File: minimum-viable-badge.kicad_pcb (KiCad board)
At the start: 2 copper layers, 120 x 64 mm, 67 parts, among them J101 EDGE_CONNECTOR, P101 USB, P102 BATTERY, P103 POT_LONG, P104 BUTTON_A, P105 BUTTON_B, P106 POT_SHORT, P107 MECH, P108 MECH, P109 MECH, P301 eInk, Q101 S8050, Q102 S8050, Q201 FDN340P, Q301 IRLML0030TRPBF, SW101 PRGM, SW102 RESET, SW201 ON|OFF, U101 ESP32-WROOM, U102 CP2102, U201 MCP73831, U202 NCP5501

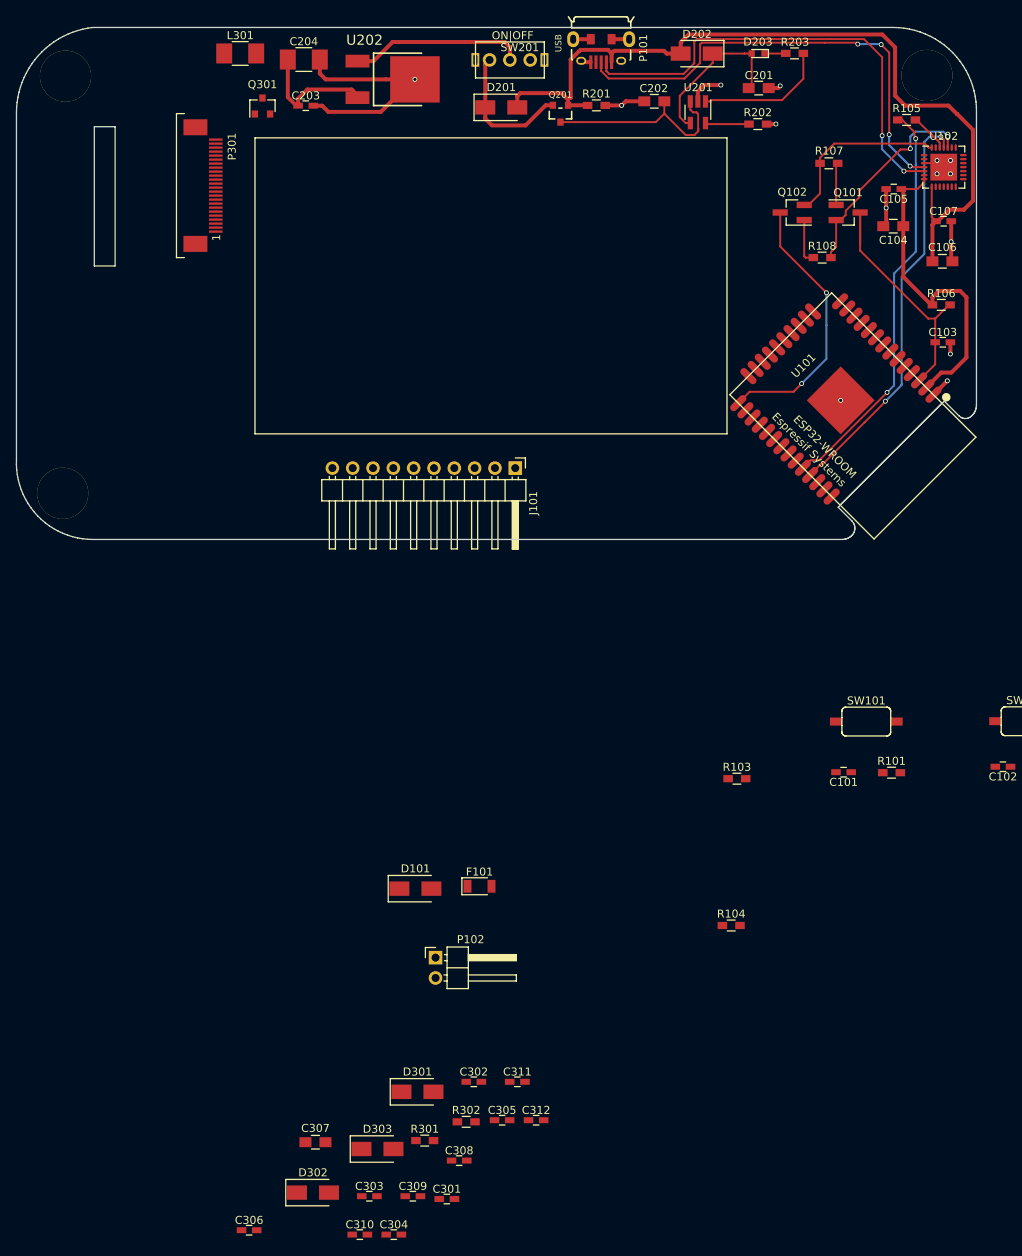
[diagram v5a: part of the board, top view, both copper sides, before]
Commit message: many more components added to the pcb
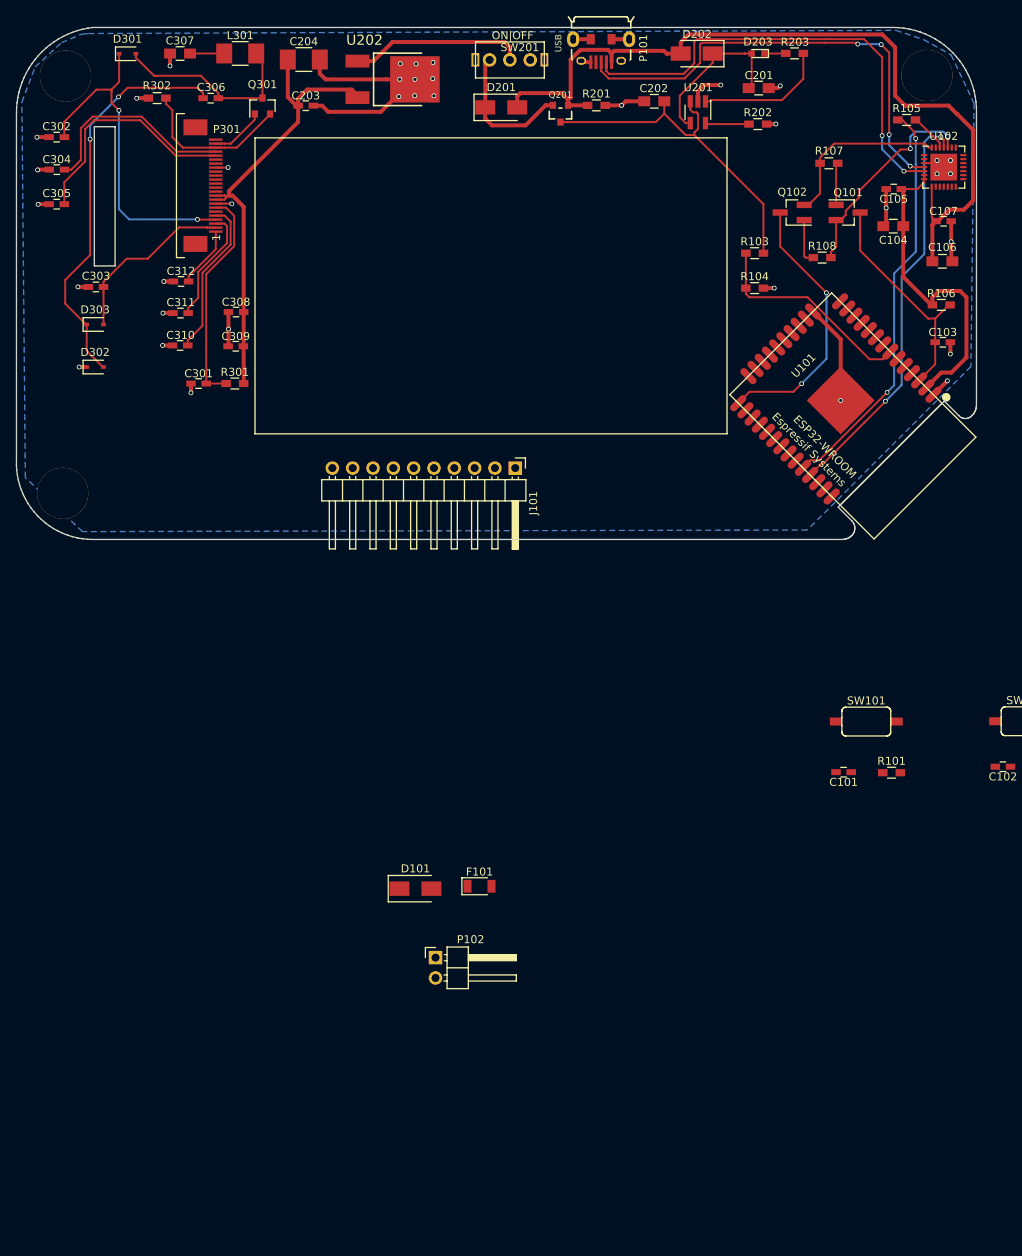
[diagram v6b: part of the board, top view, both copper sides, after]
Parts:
- D301, D302, D303: value SS14 -> SD103AWS; footprint Diodes_SMD:D_SMA -> Diodes_SMD:D_SOD-323
- moved C306 141.6 mm to (44.3, 44.8), turned to 180 degrees
- moved C304 139.6 mm to (25.1, 53.8), turned to 180 degrees
- moved C307 137.1 mm to (40.5, 39.3), turned to 180 degrees
- moved D301 134.7 mm to (33.9, 39.3)
- moved R302 133.7 mm to (37.6, 44.8), turned to 180 degrees
- moved C302 129.1 mm to (25.0, 49.7), turned to 180 degrees
- moved C305 127.3 mm to (25.0, 58.1), turned to 180 degrees
- moved C303 118.7 mm to (29.9, 68.4), turned to 180 degrees
- moved C312 113.9 mm to (40.6, 67.8), turned to 180 degrees
- moved C310 113.4 mm to (40.5, 75.8), turned to 180 degrees
- moved C308 109.7 mm to (47.5, 71.6)
- moved D303 108.9 mm to (29.8, 73.1)
- moved C309 108.5 mm to (47.4, 75.8)
- moved D302 106.7 mm to (29.8, 78.5)
- moved C301 106.6 mm to (42.8, 80.5)
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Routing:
- net Net-(C306-Pad2): track 0.00 -> 50.6 mm, vias 0 -> 2
- net +3V3: track 56.0 -> 98.8 mm
- net /E-Ink Display/PREVGH: track 0.00 -> 42.3 mm, vias 0 -> 2
- net GND: track 62.1 -> 98.4 mm, vias 14 -> 37
- net /E-Ink Display/VGH: track 0.00 -> 29.1 mm
- net /E-Ink Display/LCD_VDD: track 0.00 -> 27.6 mm
- net /BAT_MON: track 0.00 -> 26.9 mm
- net /E-Ink Display/VGL: track 0.00 -> 25.8 mm
- net Net-(C306-Pad1): track 0.00 -> 24.7 mm
- net /E-Ink Display/PREVGL: track 0.00 -> 22.2 mm
- net /E-Ink Display/VSH: track 0.00 -> 19.9 mm
- net /E-Ink Display/RESE: track 0.00 -> 19.7 mm
- net /BAT+: track 24.9 -> 43.2 mm
- net /E-Ink Display/VSL: track 0.00 -> 14.4 mm
- net /E-Ink Display/VCOM: track 0.00 -> 7.64 mm
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- added copper zone on B.Cu, net GND

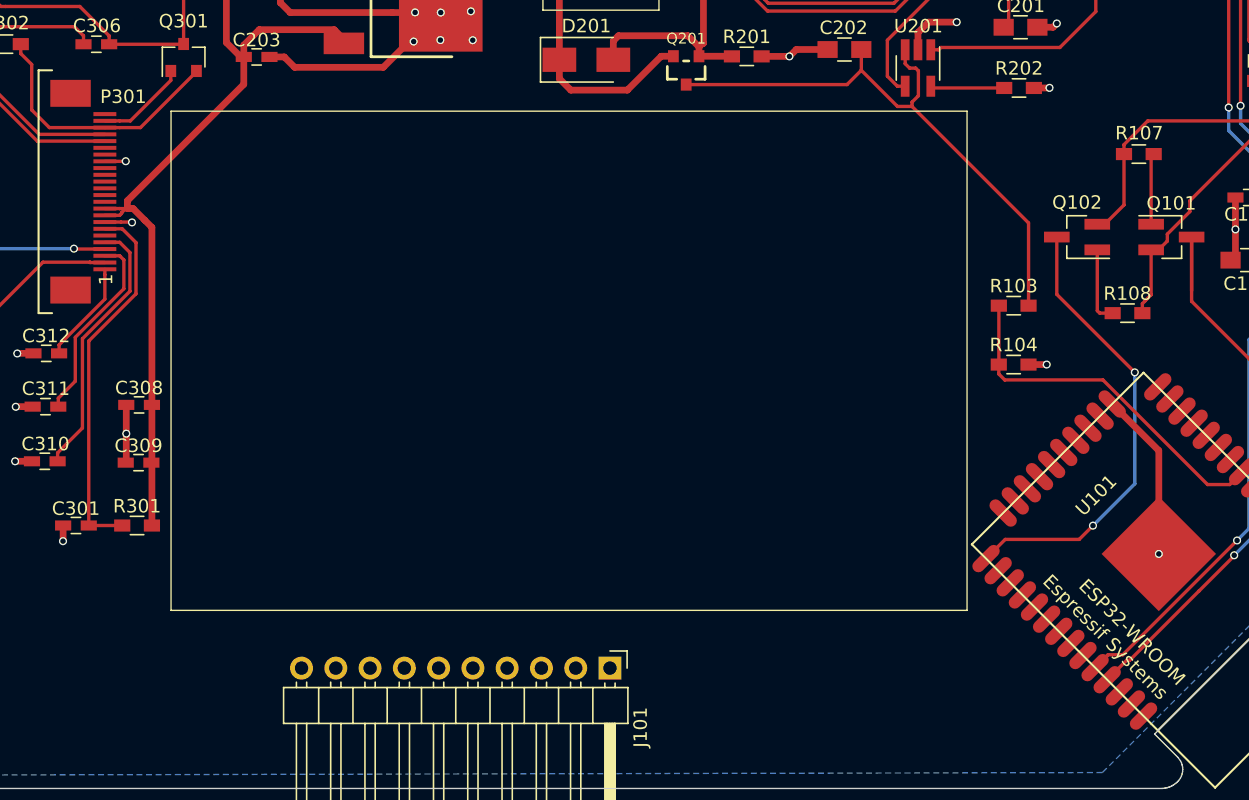
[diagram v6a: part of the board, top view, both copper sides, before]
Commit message: LCD pins routed to ESP32
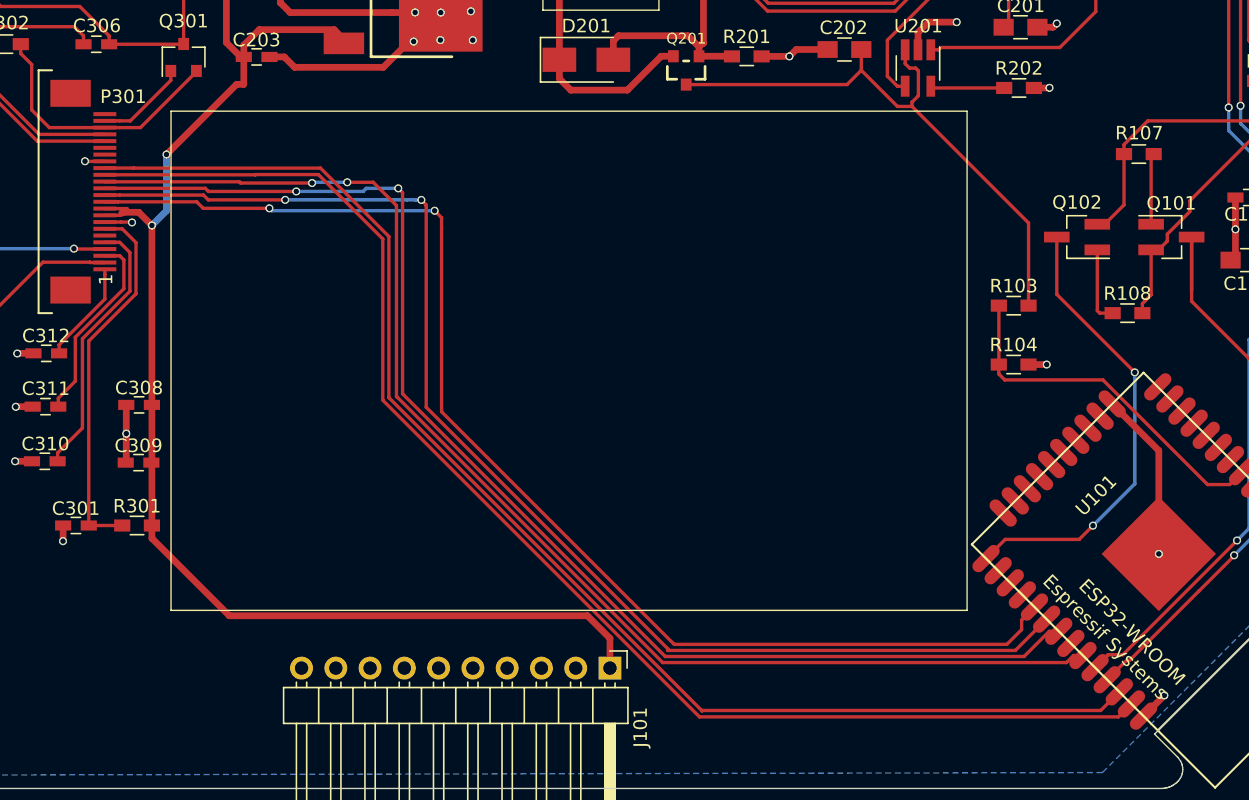
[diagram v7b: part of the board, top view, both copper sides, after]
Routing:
- net /EINK_RST: track 0.00 -> 100.1 mm
- net /EINK_BUSY: track 0.00 -> 99.4 mm
- net /EINK_D/C: track 0.00 -> 95.8 mm, vias 0 -> 2
- net /EINK_CS: track 0.00 -> 94.8 mm, vias 0 -> 2
- net /EINK_SCLK: track 0.00 -> 93.6 mm, vias 0 -> 2
- net /EINK_MOSI: track 0.00 -> 92.5 mm, vias 0 -> 2
- net +3V3: track 98.8 -> 140.2 mm, vias 0 -> 2
- net GND: track 98.4 -> 100.5 mm, vias 37 -> 38

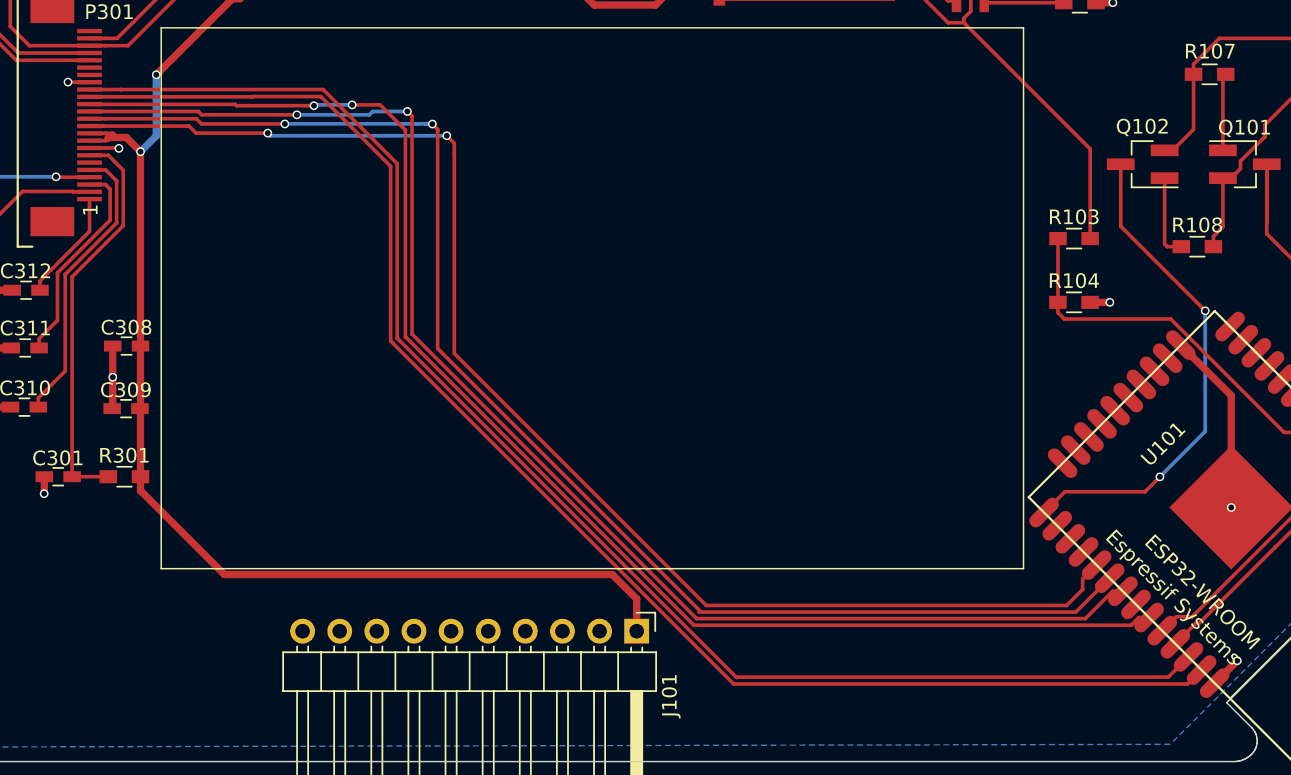
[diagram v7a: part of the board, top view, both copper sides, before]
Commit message: broken lcd routes
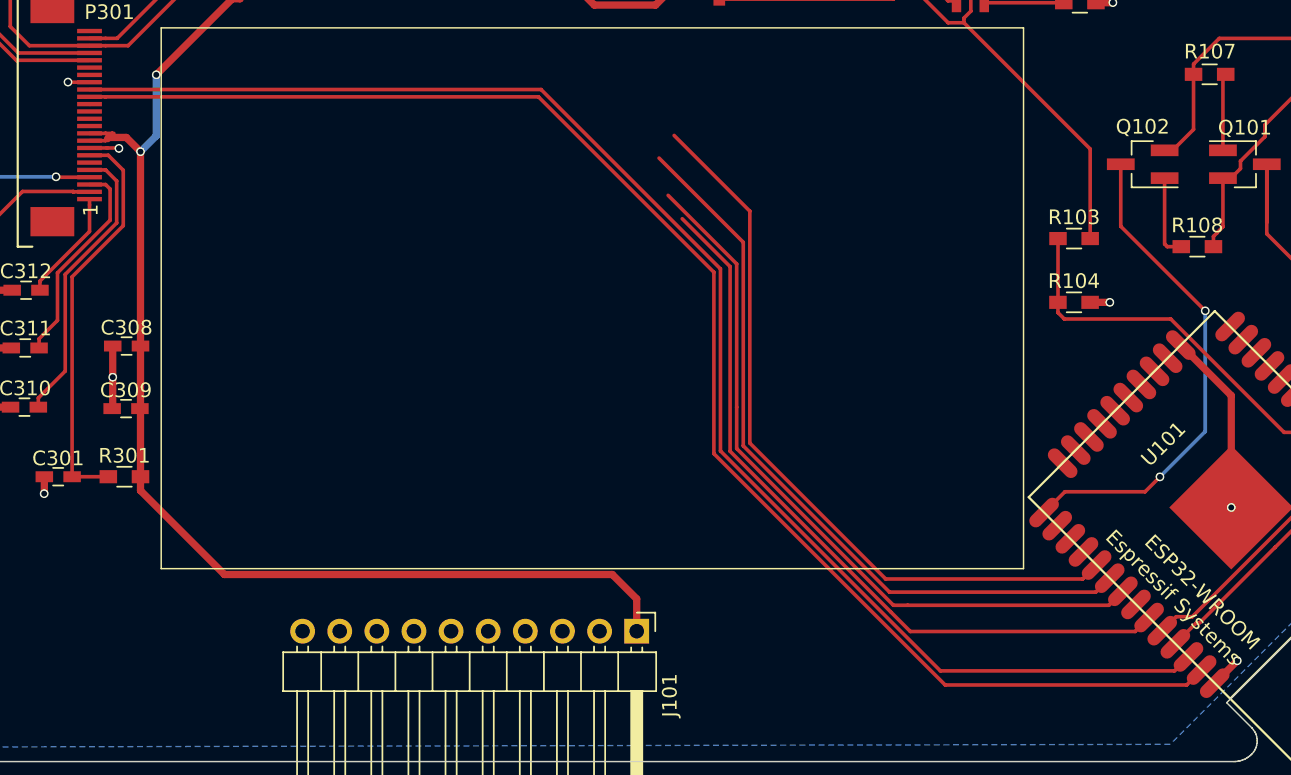
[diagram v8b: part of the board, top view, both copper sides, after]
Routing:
- net /EINK_D/C: track 95.8 -> 51.5 mm, vias 2 -> 0
- net /EINK_CS: track 94.8 -> 50.5 mm, vias 2 -> 0
- net /EINK_SCLK: track 93.6 -> 51.7 mm, vias 2 -> 0
- net /EINK_MOSI: track 92.5 -> 51.2 mm, vias 2 -> 0
